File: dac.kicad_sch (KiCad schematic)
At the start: 46 parts, among them SW3 SW_DIP_x03, SW4 SW_DIP_x03, SW5 SW_DIP_x03, SW6 SW_DIP_x03, U28 REF5030ID, U31 MCP4728, U33 MCP4728, U34 MCP4728, U35 MCP4728, U36 MCP4728, U37 MCP4728, U38 REF5050ID, U39 REF5030ID, U40 REF5050ID

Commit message: cleanup
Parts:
- added TP13, TP14, TP15, TP16, TP17, TP18: TestPoint, symbol Connector:TestPoint
- C112, C113, C114, C115: value 10u -> 1u
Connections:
- net at U33.5 (RDY/~{BSY}): now also TP14.1
- net at U34.5 (RDY/~{BSY}): now also TP15.1
- net at U35.5 (RDY/~{BSY}): now also TP16.1
- net at U36.5 (RDY/~{BSY}): now also TP17.1
- net at U37.5 (RDY/~{BSY}): now also TP18.1
- net at U31.5 (RDY/~{BSY}): now also TP13.1

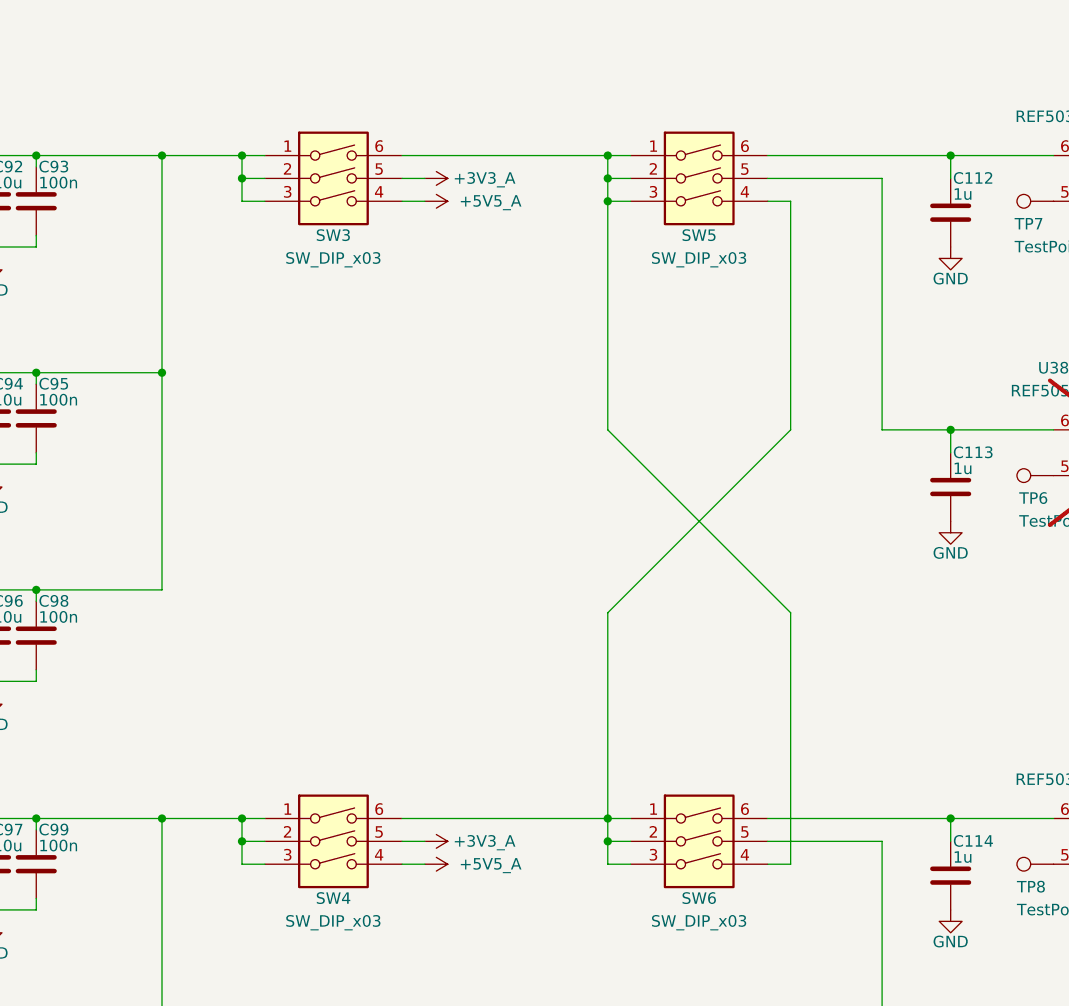
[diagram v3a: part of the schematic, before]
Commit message: annotate dip switches
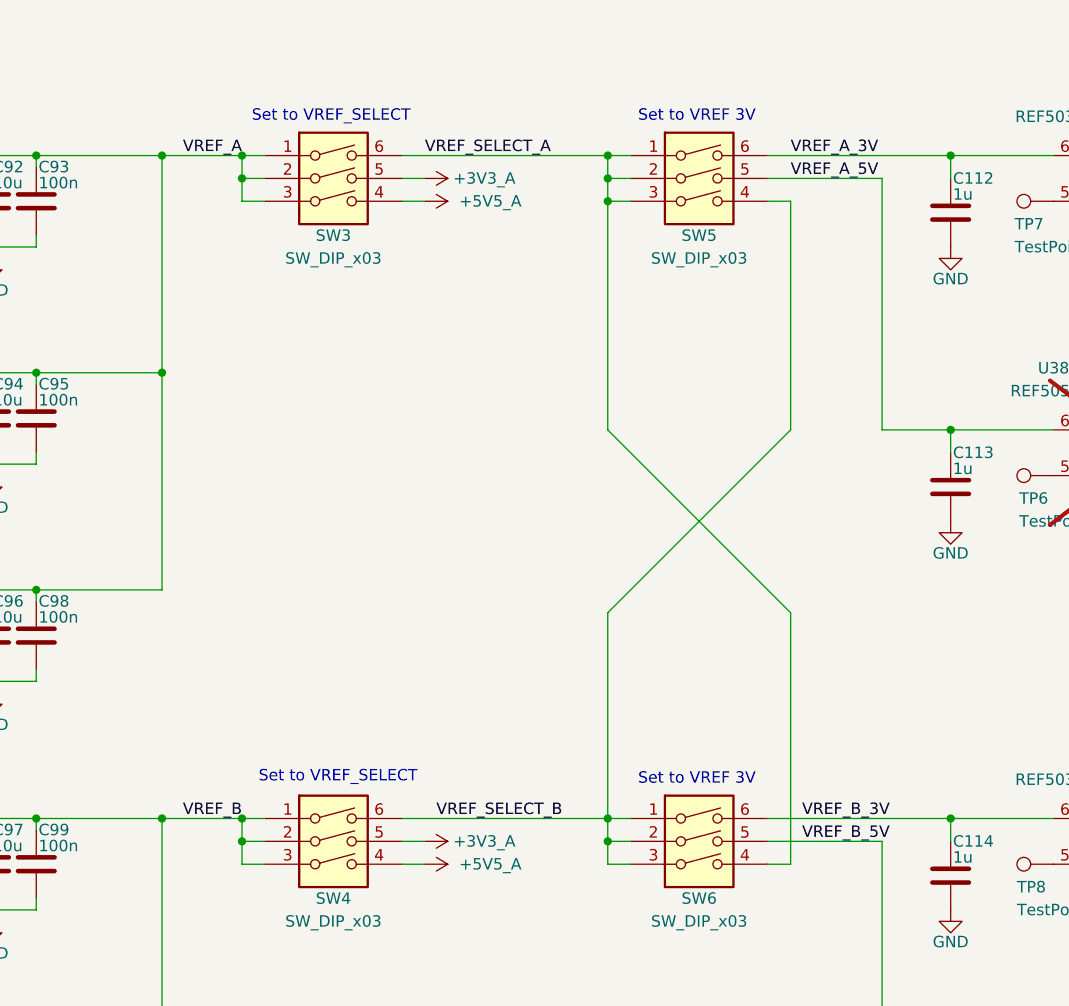
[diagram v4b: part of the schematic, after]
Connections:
- net VREF_A: now reaches C92.1, C93.1, C94.1, C95.1, C96.1, C98.1, SW3.1, SW3.2, SW3.3, U31.1 (VDD), U33.1 (VDD), U34.1 (VDD)
- net VREF_SELECT_A: now reaches SW3.6, SW5.1, SW5.2, SW5.3, SW6.4
- net VREF_A_5V: now reaches C113.1, SW5.5, U38.6 (Vout)
- net VREF_B_5V: now reaches C115.1, SW6.5, U40.6 (Vout)
- net VREF_B: now reaches C100.1, C101.1, C102.1, C103.1, C97.1, C99.1, SW4.1, SW4.2, SW4.3, U35.1 (VDD), U36.1 (VDD), U37.1 (VDD)
- net VREF_SELECT_B: now reaches SW4.6, SW5.4, SW6.1, SW6.2, SW6.3
- net VREF_B_3V: now reaches C114.1, SW6.6, U39.6 (Vout)
- net VREF_A_3V: now reaches C112.1, SW5.6, U28.6 (Vout)
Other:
- note added: "Set to VREF 3V"
- note added: "Set to VREF_SELECT"
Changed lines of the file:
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@@
 	(generator_version "9.0")
 	(paper "A4")
+	(text "Set to VREF_SELECT"
+		(exclude_from_sim no)
+		(at 149.606 35.052 0)
+		(effects
+			(font
+				(size 1.27 1.27)
+			)
+		)
+	)
+	(text "Set to VREF 3V"
+		(exclude_from_sim no)
+		(at 190.246 108.712 0)
+		(effects
+			(font
+				(size 1.27 1.27)
+			)
+		)
+	)
+	(text "Set to VREF_SELECT"
+		(exclude_from_sim no)
+		(at 150.368 108.458 0)
+		(effects
+			(font
+				(size 1.27 1.27)
+			)
+		)
+	)
+	(text "Set to VREF 3V"
+		(exclude_from_sim no)
+		(at 190.246 35.052 0)
+		(effects
+			(font
+				(size 1.27 1.27)
+			)
+		)
+	)
 	(junction
 		(at 139.7 113.03)
@@
 	(wire
 		(pts
+			(xy 139.7 113.03) (xy 130.81 113.03)
+		)
+		(stroke
+			(width 0)
+			(type default)
+		)
+	)
+	(wire
+		(pts
 			(xy 35.56 27.94) (xy 87.63 27.94)
 		)
@@
 	(wire
 		(pts
-			(xy 130.81 39.37) (xy 139.7 39.37)
-		)
-		(stroke
-			(width 0)
-			(type default)
-		)
-	)
-	(wire
-		(pts
 			(xy 116.84 113.03) (xy 130.81 113.03)
 		)
@@
 	(wire
 		(pts
-			(xy 130.81 113.03) (xy 139.7 113.03)
-		)
-		(stroke
-			(width 0)
-			(type default)
-		)
-	)
-	(wire
-		(pts
 			(xy 111.76 87.63) (xy 116.84 87.63)
 		)
@@
 	(wire
 		(pts
+			(xy 139.7 39.37) (xy 130.81 39.37)
+		)
+		(stroke
+			(width 0)
+			(type default)
+		)
+	)
+	(wire
+		(pts
 			(xy 45.72 93.98) (xy 54.61 93.98)
 		)
@@
 		)
 	)
+	(label "VREF_A_5V"
+		(at 200.66 41.91 0)
+		(effects
+			(font
+				(size 1.27 1.27)
+			)
+			(justify left bottom)
+		)
+	)
 	(label "VREF1"
 		(at 45.72 48.26 0)
@@
 		)
 	)
+	(label "VREF_B_3V"
+		(at 201.93 113.03 0)
+		(effects
+			(font
+				(size 1.27 1.27)
+			)
+			(justify left bottom)
+		)
+	)
 	(label "VREF11"
 		(at 45.72 101.6 0)
@@
 		)
 	)
+	(label "VREF_B"
+		(at 139.7 113.03 180)
+		(effects
+			(font
+				(size 1.27 1.27)
+			)
+			(justify right bottom)
+		)
+	)
 	(label "~{LDAC}2"
 		(at 102.87 99.06 180)
@@
 		)
 	)
+	(label "VREF_SELECT_A"
+		(at 160.02 39.37 0)
+		(effects
+			(font
+				(size 1.27 1.27)
+			)
+			(justify left bottom)
+		)
+	)
 	(label "VREF16"
 		(at 45.72 143.51 0)
@@
 		)
 	)
+	(label "VREF_A_3V"
+		(at 200.66 39.37 0)
+		(effects
+			(font
+				(size 1.27 1.27)
+			)
+			(justify left bottom)
+		)
+	)
 	(label "VREF19"
 		(at 45.72 151.13 0)
@@
 		)
 	)
+	(label "VREF_SELECT_B"
+		(at 161.29 113.03 0)
+		(effects
+			(font
+				(size 1.27 1.27)
+			)
+			(justify left bottom)
+		)
+	)
 	(label "VREF6"
 		(at 45.72 74.93 0)
@@
 		)
 	)
+	(label "VREF_A"
+		(at 139.7 39.37 180)
+		(effects
+			(font
+				(size 1.27 1.27)
+			)
+			(justify right bottom)
+		)
+	)
 	(label "VREF20"
 		(at 45.72 167.64 0)
@@
 		(effects
 			(font
+				(size 1.27 1.27)
+			)
+			(justify left bottom)
+		)
+	)
+	(label "VREF_B_5V"
+		(at 201.93 115.57 0)
+		(effects
+			(font
